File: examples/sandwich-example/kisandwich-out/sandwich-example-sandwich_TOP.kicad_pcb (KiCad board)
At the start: 4 copper layers, 100 x 80 mm, 1 part, among them U2 LM555xM

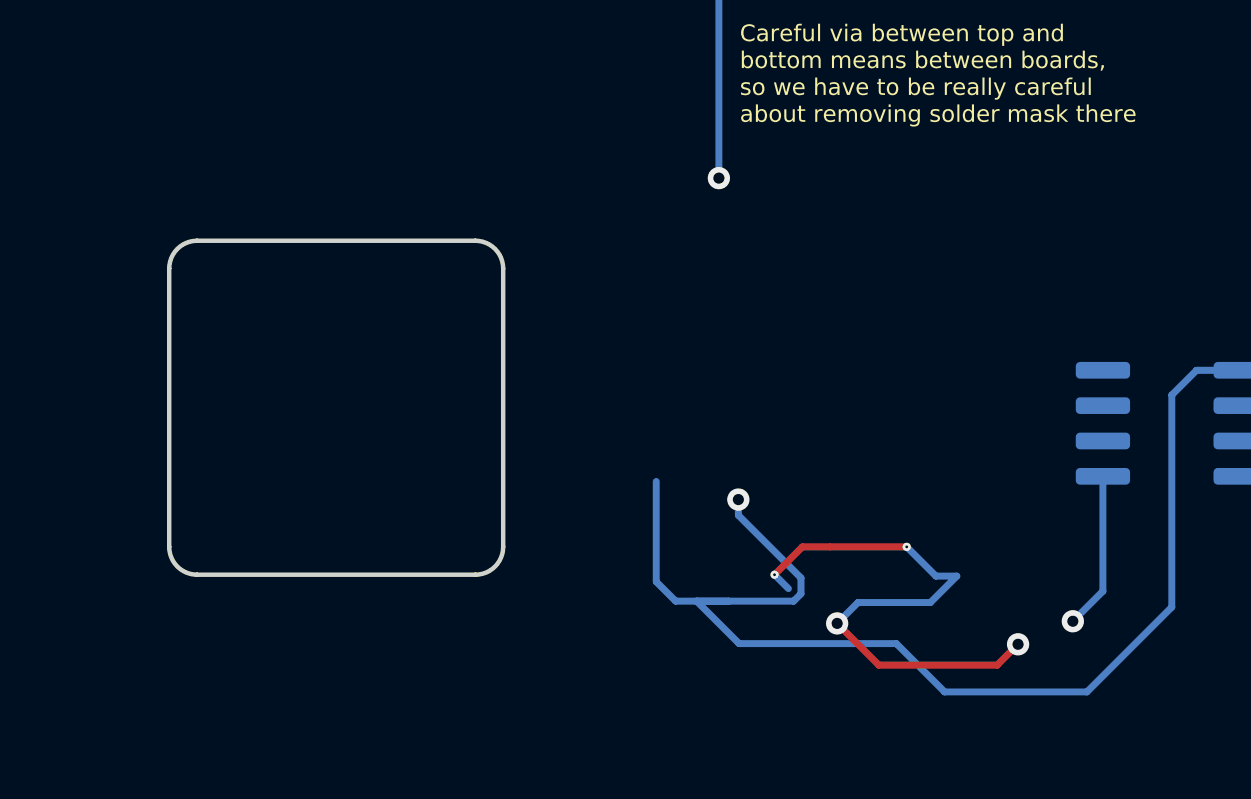
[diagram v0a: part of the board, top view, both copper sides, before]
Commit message: Updated basic example to v6 standard directory format
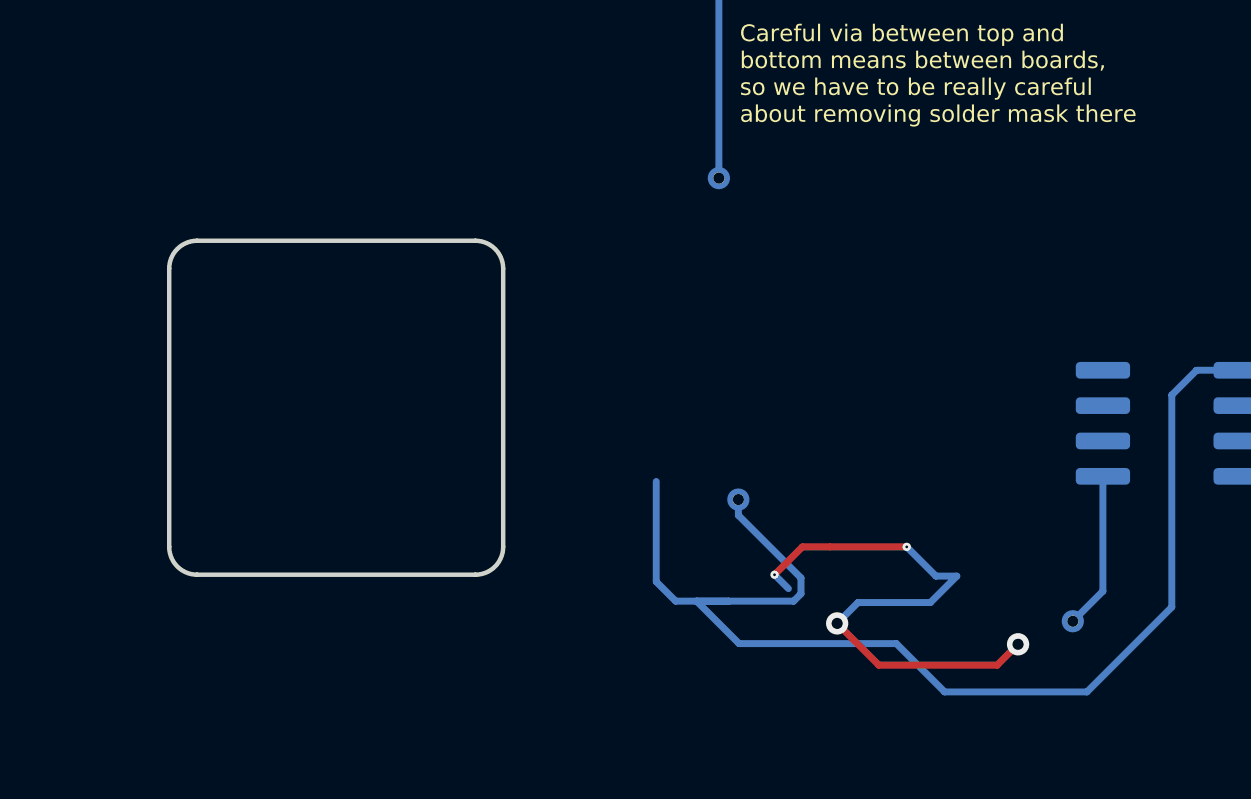
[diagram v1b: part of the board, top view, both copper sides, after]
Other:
- net class Default removed
